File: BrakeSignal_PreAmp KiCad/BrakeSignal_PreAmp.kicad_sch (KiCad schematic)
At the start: 14 parts, among them IC14 TLV9062QDGKRQ1, IC2 LM339LVDR, IC9 TLV9062QDGKRQ1, J1 4P Droit 22-11-2042, J2 Conn_01x02

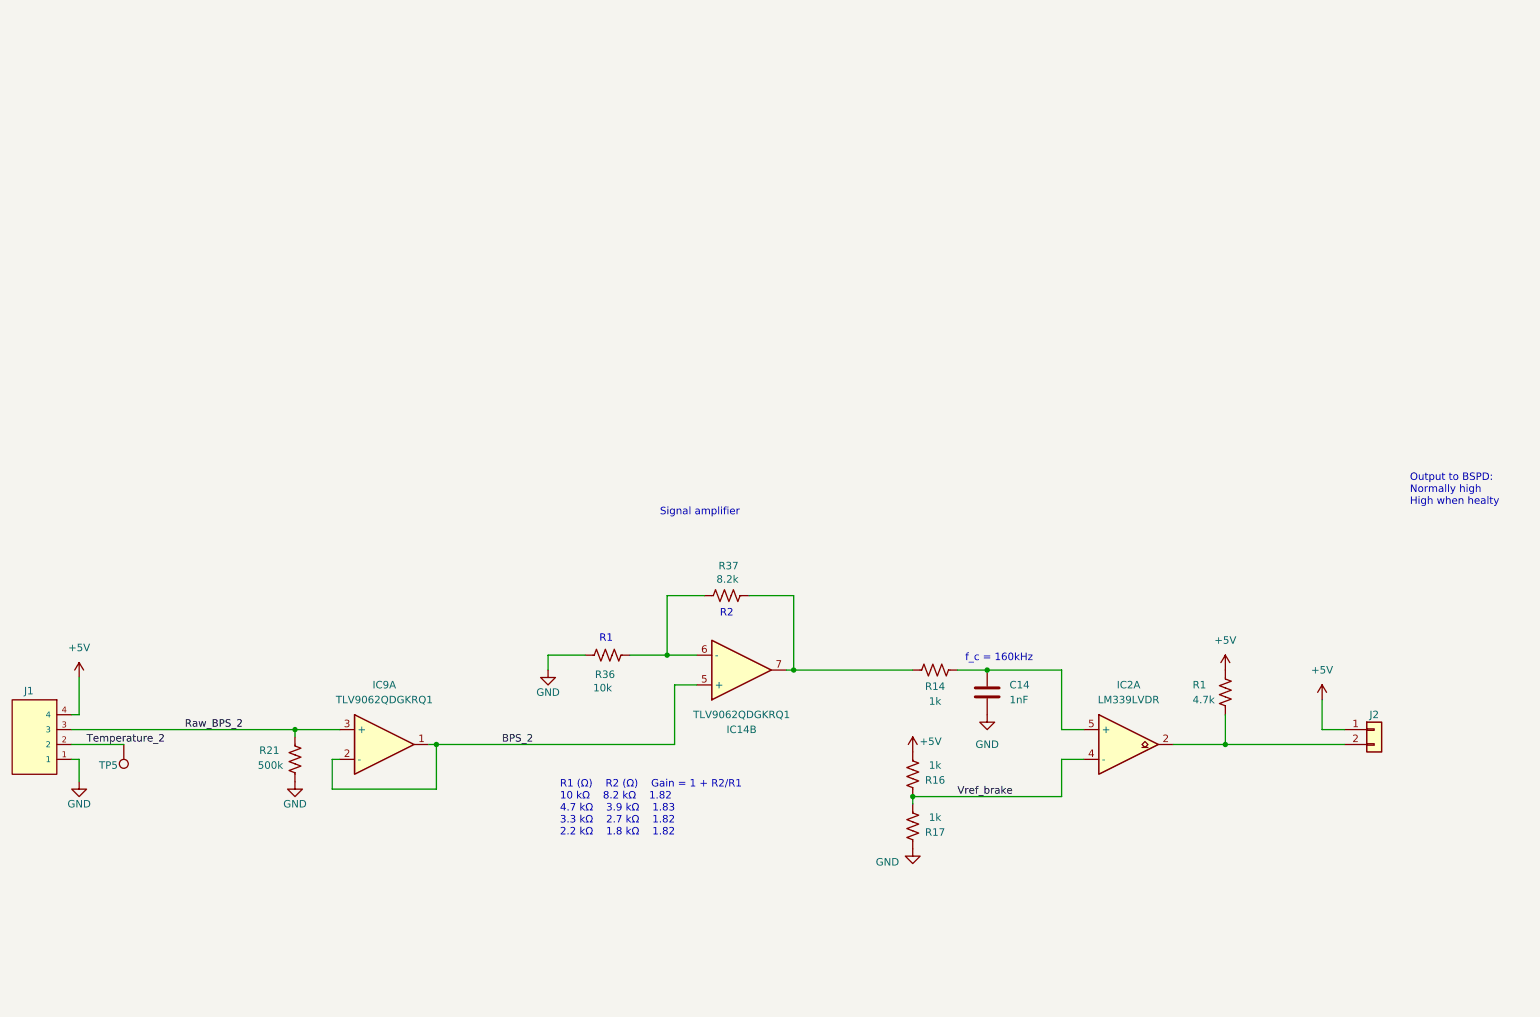
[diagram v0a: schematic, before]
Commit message: Schematic done
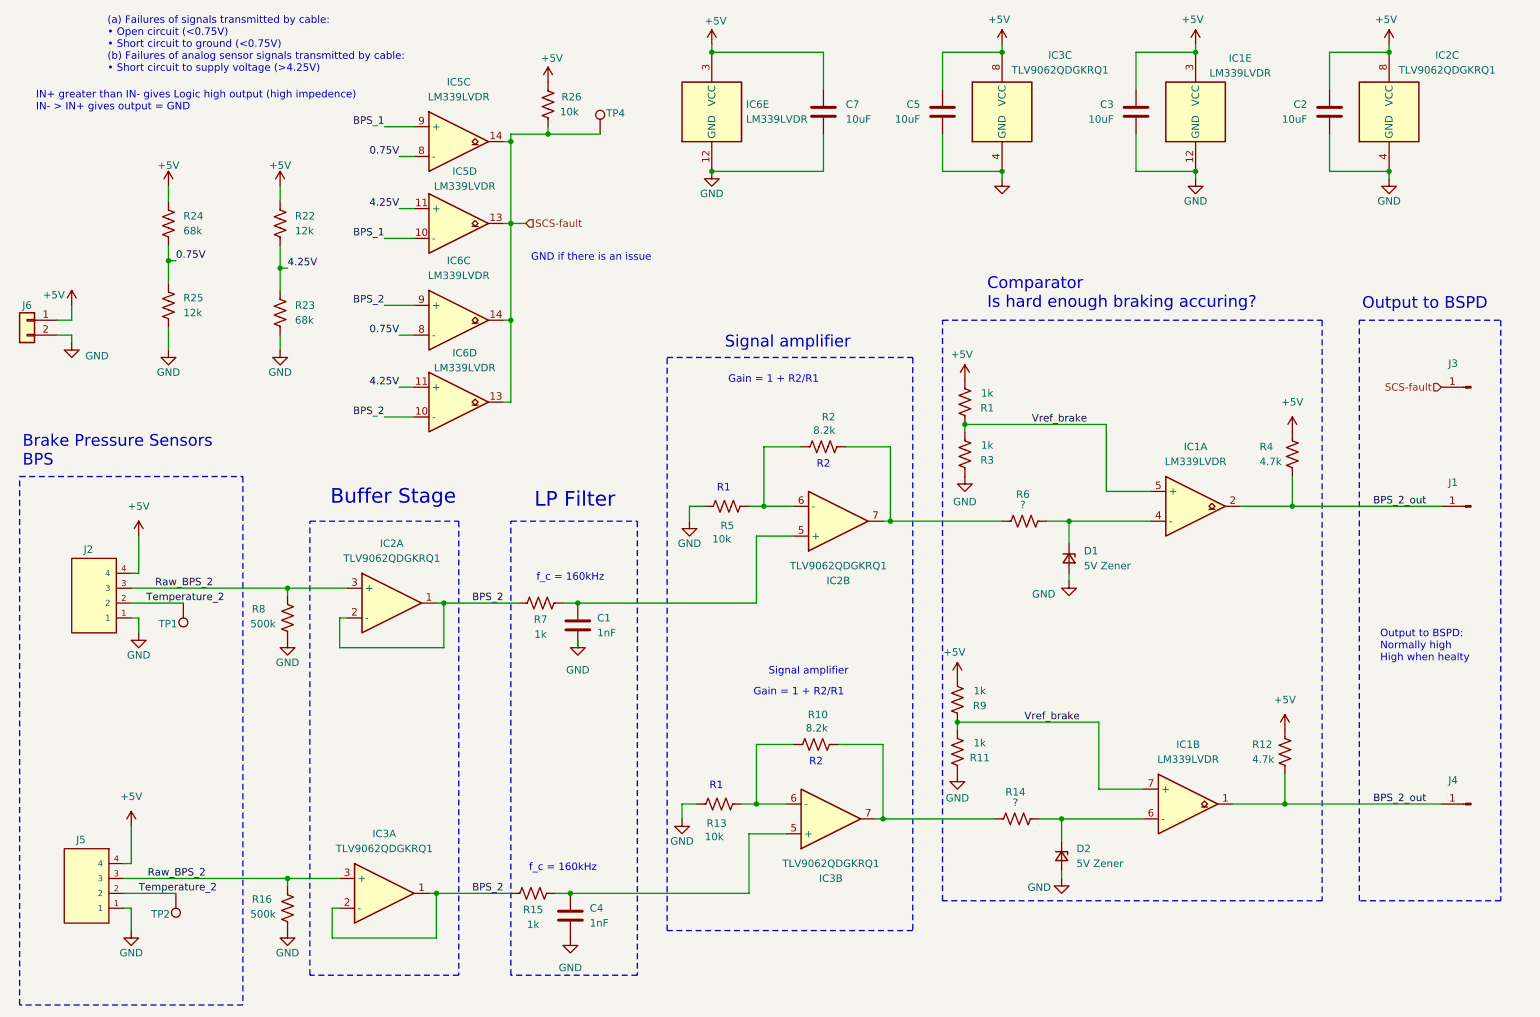
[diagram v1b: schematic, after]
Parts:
- removed C14: 1nF, Capacitor_SMD:C_0805_2012Metric, symbol Device:C
- removed J2: Conn_01x02, Connector_JST:JST_XH_B2B-XH-A_1x02_P2.50mm_Vertical, symbol LEM_HAS_100-S:Conn_01x02
- added C1, C4: 1nF, Capacitor_SMD:C_0805_2012Metric, symbol Device:C
- added C2, C3, C5, C7: 10uF, Capacitor_SMD:C_0603_1608Metric, symbol Device:C
- added D1, D2: 5V Zener, symbol Device:D_Zener_Small
- added unit 5 of IC1
- added unit 1 of IC1
- added IC2: TLV9062QDGKRQ1, LIB_TLV9062QDGKRQ1:SOP65P490X110-8N, symbol TLV9062QDGKRQ1:TLV9062QDGKRQ1
- added unit 3 of IC3
- added IC5, IC6: LM339LVDR, SOIC127P600X175-14N, symbol LM339LVDR:LM339LVDR
- added J1, J3, J4: Conn_01x01_Pin, Connector_PinSocket_2.54mm:PinSocket_1x01_P2.54mm_Vertical, symbol Connector:Conn_01x01_Pin
- added J2: 4P Droit 22-11-2042, Connector_JST:JST_XH_B4B-XH-A_1x04_P2.50mm_Vertical, symbol EPSA_lib:4P Droit 22-11-2042
- added J6: Conn_01x02, Connector_JST:JST_XH_B2B-XH-A_1x02_P2.50mm_Vertical, symbol LEM_HAS_100-S:Conn_01x02
- added R1, R15, R3, R7: 1k, Resistor_SMD:R_0805_2012Metric, symbol Device:R_US
- added R2: 8.2k, Resistor_SMD:R_0805_2012Metric, symbol Device:R_US
- added R22, R25: 12k, Resistor_SMD:R_0805_2012Metric, symbol Device:R_US
- added R23, R24: 68k, Resistor_SMD:R_0805_2012Metric, symbol Device:R_US
- added R26, R5: 10k, Resistor_SMD:R_0805_2012Metric, symbol Device:R_US
- added R4: 4.7k, Resistor_SMD:R_0805_2012Metric, symbol Device:R_US
- added R6: ?, Resistor_SMD:R_0805_2012Metric, symbol Device:R_US
- added R8: 500k, Resistor_SMD:R_0805_2012Metric, symbol Device:R_US
- added TP1, TP4: TestPoint, TestPoint:TestPoint_Pad_D1.5mm, symbol Connector:TestPoint
- R14: value 1k -> ?
- renumbered IC2 to IC1, IC9 to IC3, IC14 to IC3, J1 to J5, R37 to R10, R17 to R11, R1 to R12, R36 to R13, R21 to R16, R16 to R9, TP5 to TP2
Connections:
- net +5V: now also C2.1, C3.1, C5.1, C7.1, IC1.3 (VCC), IC2.8 (VCC), IC3.8 (VCC), IC6.3 (VCC), J2.4, J6.1 (Pin_1), R1.2, R22.1, R24.1, R26.1, R4.1
- net BPS_2: now also IC2.1, IC2.2 (-), IC6.10 (-), IC6.9 (+), R15.1, R7.1; no longer IC3.5 (+)
- net GND: now also C1.2, C2.2, C3.2, C4.2, C5.2, C7.2, D1.2 (A), D2.2 (A), IC1.12 (GND), IC2.4 (GND), IC3.4 (GND), IC6.12 (GND), J2.1, J6.2 (Pin_2), R23.2, R25.2, R3.1, R5.1, R8.2
- net Raw_BPS_2: now also IC2.3 (+), J2.3, R8.1
- net Temperature_2: now also J2.2, TP1.1
- net Vref_brake: now also IC1.7 (+), IC1.5 (+), R1.1, R3.2; no longer IC1.4 (-)
- net at R14.2: now also IC3.7, R10.2; no longer IC1.5 (+)
- net BPS_2_out: now reaches R12.2
- net BPS_2_out: now also IC1.1, IC1.2, J1.1 (Pin_1), J4.1 (Pin_1), R4.2; no longer IC1.2
- new net: C4.1, IC3.5 (+), R15.2
- new net: C1.1, IC2.5 (+), R7.2
- new net: D1.1 (K), IC1.4 (-), R6.1
- new net: IC2.6 (-), R2.1, R5.2
- new net: IC2.7, R2.2, R6.2
- new net: D2.1 (K), IC1.6 (-), R14.1
- new net 0.75V: IC5.8 (-), IC6.8 (-), R24.2, R25.1
- new net 4.25V: IC5.11 (+), IC6.11 (+), R22.2, R23.1
- new net BPS_1: IC5.10 (-), IC5.9 (+)
- new net SCS-fault: IC5.13, IC5.14, IC6.13, IC6.14, J3.1 (Pin_1), R26.2, TP4.1
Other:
- note added: "(a) Failures of signals transmitted by cable: • Open circuit (<0.75V) • Short circuit to ground (<0.75V) (b) Failures of analog sensor signals transmitted by cable: • Short circuit to supply voltage (>4.25V)"
- note added: "Brake Pressure Sensors BPS"
- note added: "Buffer Stage"
- note added: "Comparator Is hard enough braking accuring?"
- note added: "GND if there is an issue"
- note added: "Gain = 1 + R2/R1"
- note added: "IN+ greater than IN- gives Logic high output (high impedence) IN- > IN+ gives output = GND"
- note added: "LP Filter"
- note added: "Output to BSPD"
- note removed: "R1 (Ω) R2 (Ω) Gain = 1 + R2/R1 10 kΩ 8.2 kΩ 1.82 4.7 kΩ 3.9 kΩ 1.83 3.3 kΩ 2.7 kΩ 1.82 2.2 kΩ 1.8 kΩ 1.82"
- moved on the sheet: IC1B, IC3A, IC3B, J5, R10, R11, R12, R13, R16, R9, TP2

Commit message: Routing done, no errors. Zener missing
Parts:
- renumbered IC6 to IC5
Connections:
- net 0.75V: now also IC5.6 (-); no longer IC5.8 (-)
- net 4.25V: now also IC5.5 (+); no longer IC5.11 (+)
- net BPS_1: now also IC2.1, IC2.2 (-), IC5.4 (-), IC5.7 (+), R7.1; no longer IC5.10 (-), IC5.9 (+)
- net BPS_2: no longer IC2.1, IC2.2 (-), R7.1
- net BPS_2_out: no longer IC1.2, J1.1 (Pin_1), R4.2
- net Raw_BPS_2: now also J5.2; no longer IC2.3 (+), J2.3, J5.3, R8.1
- net SCS-fault: now also IC5.1, IC5.2; no longer IC5.13, IC5.14
- net Temperature_2: now also J5.3; no longer J2.2, J5.2, TP1.1
- new net BPS_1_out: IC1.2, J1.1 (Pin_1), R4.2
- new net Raw_BPS_1: IC2.3 (+), J2.2, R8.1
- new net Temperature_1: J2.3, TP1.1
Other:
- note added: "Brake Pressure Sensors (BPS)"
- note added: "Comparator Is hard enough braking accuring? Output low if yes"
- note added: "Takes in the raw signal from the brake pressure sensors (BPS). Amplifies the signal Converts analog signal to digital Outputs low when hard braking"
- note removed: "Brake Pressure Sensors BPS"
- note removed: "Comparator Is hard enough braking accuring?"
- company: (none) -> Axel Jönehag
- title: (none) -> BSPD PreAmp
- moved on the sheet: C7, D2, IC1B, IC5E, J2, J5, R11, R12, R14, R26, R9, TP1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
